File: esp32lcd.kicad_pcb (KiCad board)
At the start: 2 copper layers, 78 x 44 mm, 26 parts, among them J101 USB_B_Micro, J102 Barrel_Jack_Switch, Q102 MMBT5551, Q103 MMBT5551, Q107 MMBT5401, U101 SRV05-4, U102 CH340C, U105 AMS1117-3.3, U106 ESP32-WROOM-32D, U107 ILI9341_SPI_Touch_SD

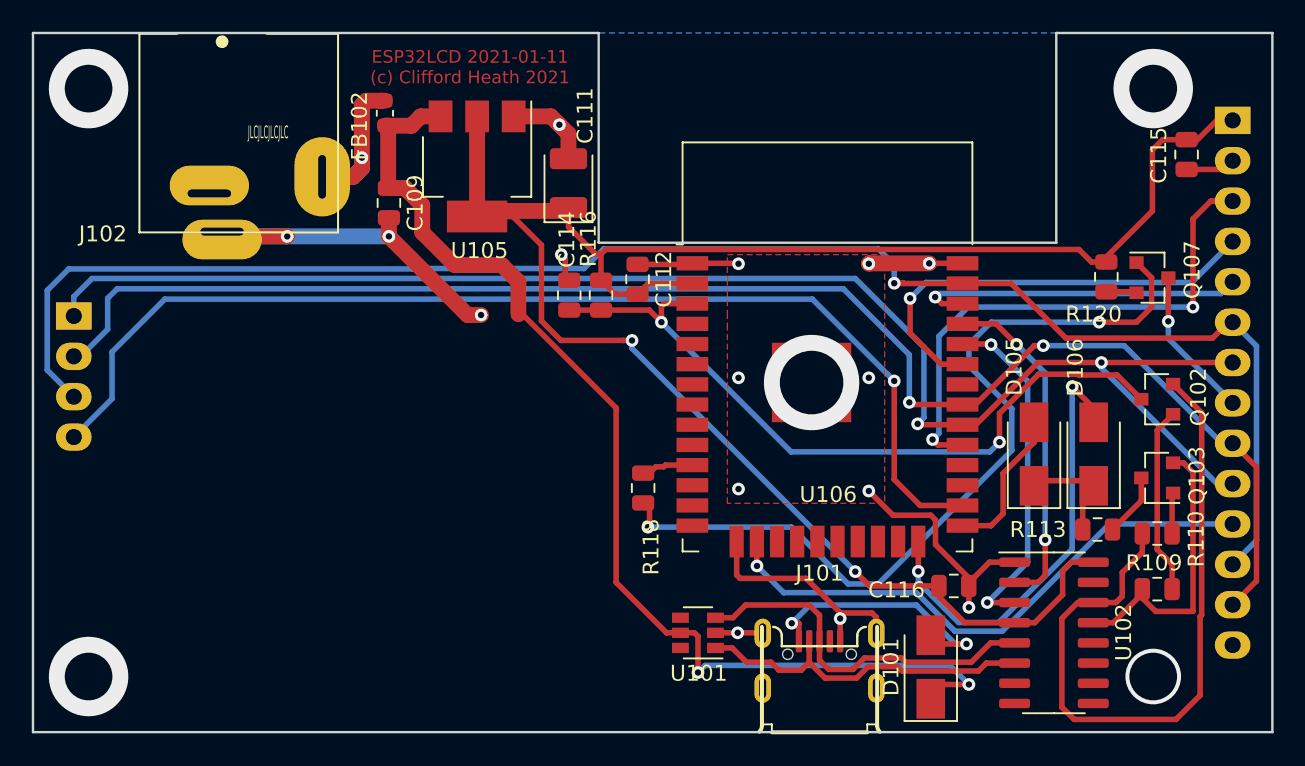
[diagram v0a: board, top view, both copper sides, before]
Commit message: Switched TxD and RxD between the two chips
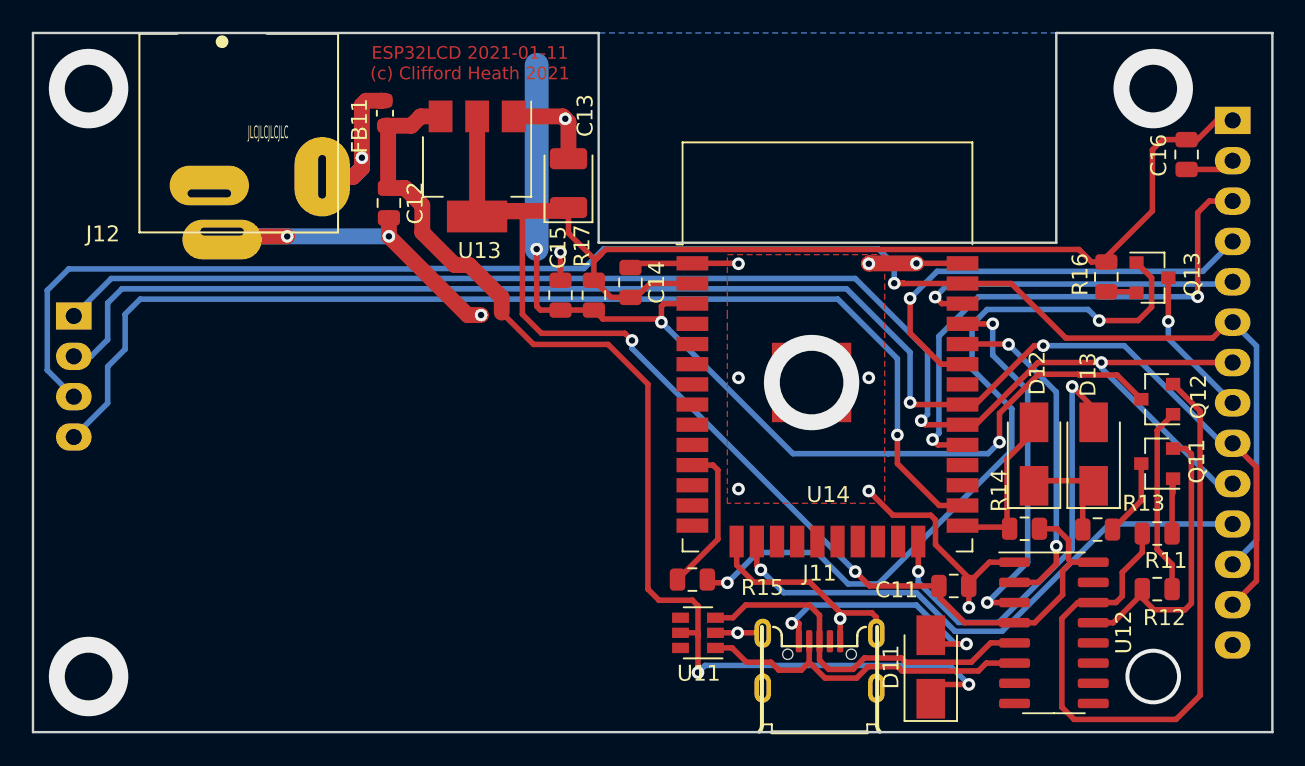
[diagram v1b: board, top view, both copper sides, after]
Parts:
- removed D105: SS14, Diode_SMD:D_SMA
- removed R109, R113: 10k, Resistor_SMD:R_0805_2012Metric
- added D12: SS14, Diode_SMD:D_SMA, F.Cu at (138.0, 137.5)
- added R12: 10k, Resistor_SMD:R_0805_2012Metric, F.Cu at (145.8, 146.0)
- added R13: 10k, Resistor_SMD:R_0805_2012Metric, F.Cu at (142.0, 142.2)
- added R14: 10k, Resistor_SMD:R_0805_2012Metric, F.Cu at (137.4, 142.2)
- moved R15 6.54 mm to (116.5, 145.4), turned to 0 degrees
- moved Q11 0.90 mm to (145.8, 138.1)
- moved C15 0.55 mm to (108.2, 127.5)
- moved C14 0.49 mm to (112.6, 126.7)
- moved R17 0.45 mm to (110.3, 127.5)
- renumbered C116 to C11, C109 to C12, C111 to C13, C112 to C14, C114 to C15, C115 to C16, D101 to D11, D106 to D13, FB102 to FB11, J101 to J11, J102 to J12, Q103 to Q11, Q102 to Q12, Q107 to Q13, R110 to R11, R118 to R15, R120 to R16, R116 to R17, U101 to U11, U102 to U12, U105 to U13, U106 to U14, U107 to U15
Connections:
- U12 pad 2: /TXD0 -> /RXD0
- U12 pad 3: /RXD0 -> /TXD0
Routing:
- net ESP_EN: track 46.7 -> 63.6 mm, vias 2 -> 3
- net Net-(R15-Pad1): track 2.91 -> 9.68 mm
- net +3V3: track 126.1 -> 132.0 mm
- net Net-(Q13-Pad1): track 52.9 -> 48.8 mm
- net +5V: track 69.8 -> 72.5 mm
- net /TXD0: track 21.3 -> 23.1 mm
- net Net-(Q11-Pad1): track 2.58 -> 4.38 mm
- net VSPICS1: track 70.3 -> 71.4 mm
- net Net-(D12-Pad2): track 9.43 -> 10.5 mm
- net VSPICLK: track 95.1 -> 94.1 mm
- net Net-(Q11-Pad3): track 4.00 -> 4.90 mm
- net /RXD0: track 21.8 -> 21.1 mm
- net GND: track 86.4 -> 87.0 mm

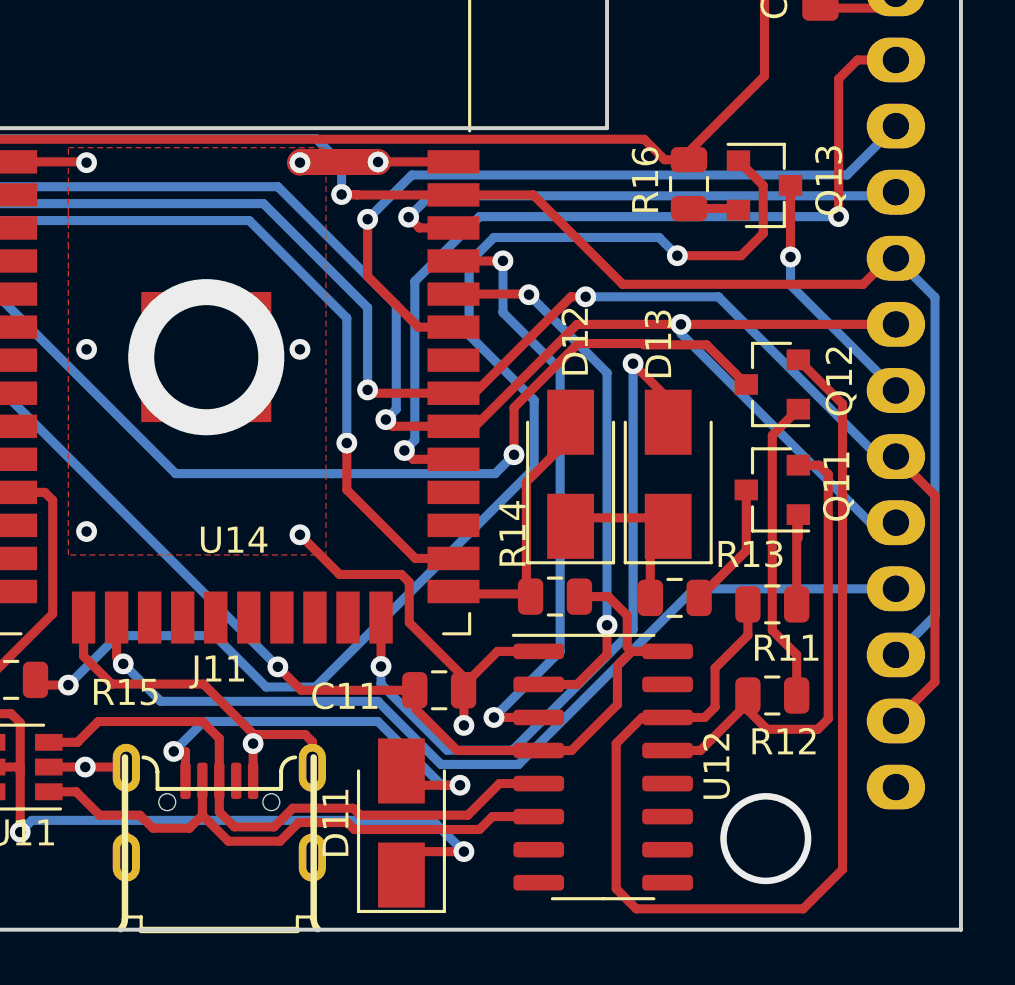
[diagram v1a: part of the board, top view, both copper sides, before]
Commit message: Ditched diode steering in favour of another transistor
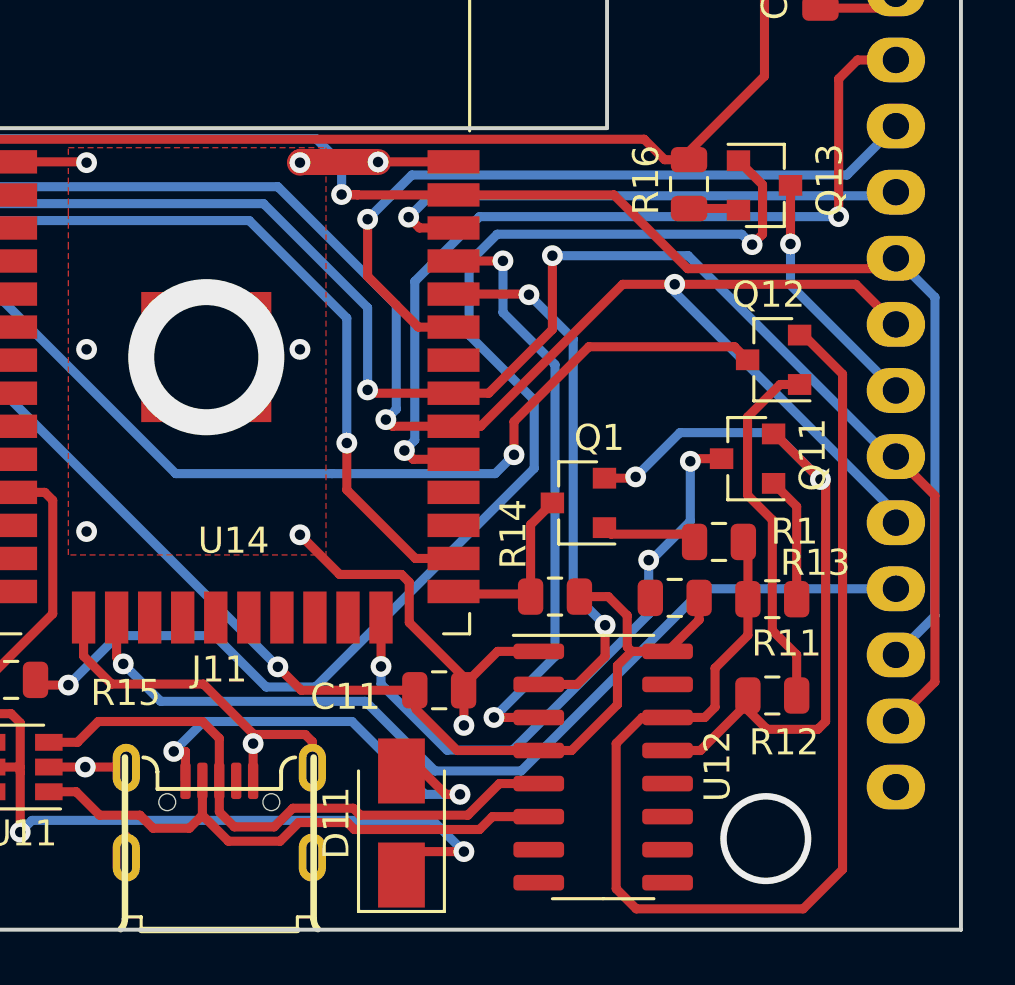
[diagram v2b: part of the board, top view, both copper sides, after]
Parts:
- removed D12, D13: SS14, Diode_SMD:D_SMA
- added Q1: MMBT5551, cjh_jlcpcb:SOT-23, F.Cu at (138.3, 138.6)
- added R1: 10k, Resistor_SMD:R_0805_2012Metric, F.Cu at (143.7, 140.1)
- R13, R14: value 10k -> 100k
- moved Q11 1.53 mm to (144.8, 136.9)
- moved Q12 0.95 mm to (145.8, 133.1)
- moved R11 0.20 mm to (145.8, 142.3)
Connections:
- R13 pad 1: Net-(Q11-Pad3) -> +3V3
- R13 pad 2: Net-(D12-Pad1) -> Net-(Q11-Pad3)
- U14 pad 24: Net-(D13-Pad2) -> Net-(Q11-Pad3)
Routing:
- net Net-(D13-Pad2): track 28.2 -> 0.00 mm, vias 2 -> 0
- net Net-(Q11-Pad3): track 4.90 -> 23.9 mm, vias 0 -> 3
- net Net-(Q1-Pad2): track 18.9 -> 30.1 mm, vias 0 -> 2
- net Net-(D12-Pad1): track 7.05 -> 0.00 mm
- net Net-(Q1-Pad1): track 0.00 -> 3.69 mm
- net Net-(Q12-Pad2): track 44.4 -> 47.9 mm
- net Net-(Q1-Pad3): track 10.5 -> 7.22 mm
- net VSPIDIN: track 96.4 -> 99.4 mm
- net +3V3: track 132.0 -> 134.6 mm
- net VSPICLK: track 94.1 -> 96.4 mm
- net Net-(Q12-Pad1): track 11.8 -> 14.0 mm
- net ESP_EN: track 63.6 -> 62.8 mm
- net Net-(Q11-Pad1): track 4.38 -> 5.02 mm

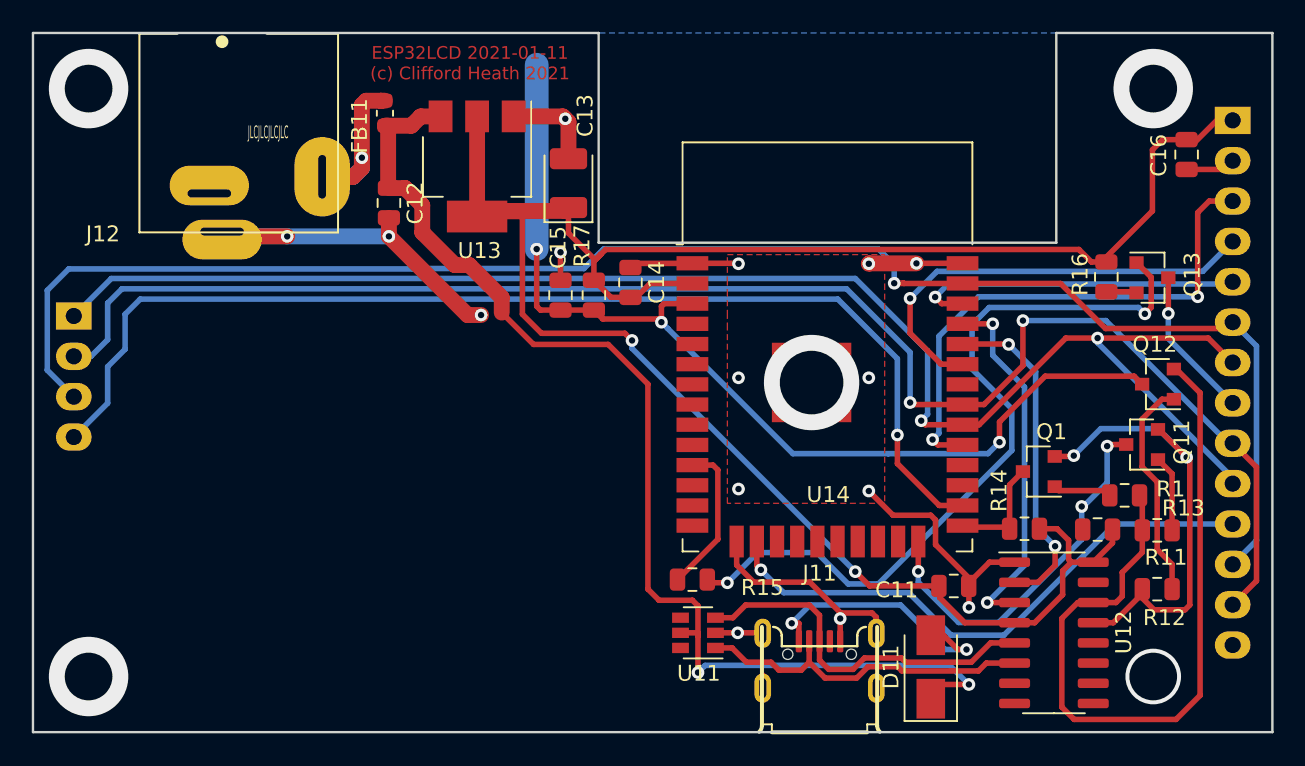
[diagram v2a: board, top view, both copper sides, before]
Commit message: Deleted GPIO2 boot pulldown
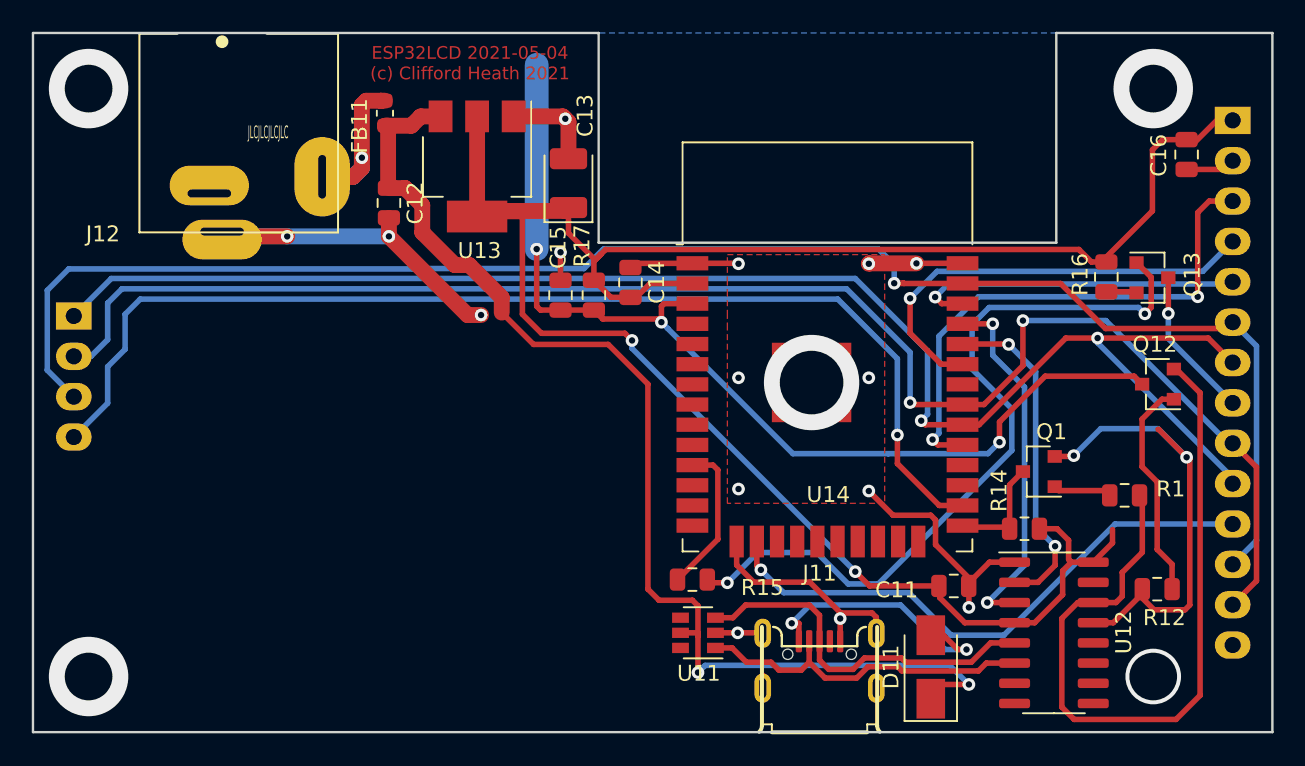
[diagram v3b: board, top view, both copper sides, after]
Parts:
- removed Q11: MMBT5551, cjh_jlcpcb:SOT-23
- removed R11: 10k, Resistor_SMD:R_0805_2012Metric
- removed R13: 100k, Resistor_SMD:R_0805_2012Metric
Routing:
- net Net-(U14-Pad24): track 23.9 -> 0.00 mm, vias 3 -> 0
- net Net-(Q11-Pad1): track 5.02 -> 0.00 mm
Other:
- board text added: "ESP32LCD 2021-05-04 (c) Clifford Heath 2021"
- board text removed: "ESP32LCD 2021-01-11 (c) Clifford Heath 2021"

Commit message: Updated to add JTAG debug
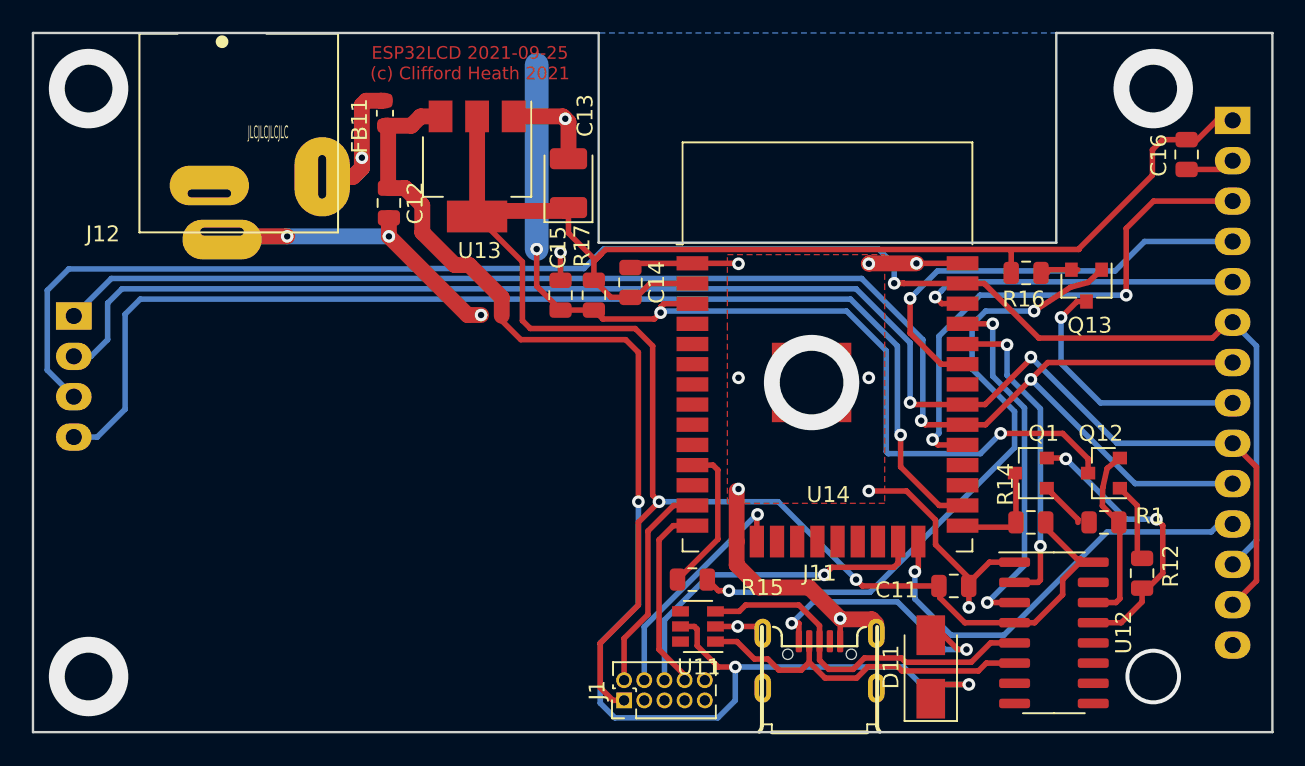
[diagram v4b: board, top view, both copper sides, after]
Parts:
- added J1: Conn_02x05_Odd_Even, Connector_PinHeader_1.27mm:PinHeader_2x05_P1.27mm_Vertical, F.Cu at (112.2, 153.0)
- moved Q12 6.55 mm to (142.4, 138.7)
- moved R16 5.06 mm to (137.5, 126.1), turned to 180 degrees
- moved Q13 4.18 mm to (141.3, 126.9), turned to 90 degrees
- moved R1 2.14 mm to (142.4, 141.8)
- moved R12 1.38 mm to (144.8, 145.0), turned to 90 degrees
- moved R14 0.57 mm to (137.8, 141.8)
- moved Q1 0.51 mm to (137.8, 138.7)
- moved U11 0.40 mm to (116.8, 148.3)
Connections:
- U14 pad 16: VSPICS2 -> Net-(J1-Pad4)
- U14 pad 24: Net-(U14-Pad24) -> VSPICS2
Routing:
- net Net-(Q12-Pad2): track 47.9 -> 11.5 mm
- net Net-(J1-Pad6): track 0.00 -> 21.3 mm, vias 0 -> 1
- net +3V3: track 134.6 -> 150.3 mm
- net Net-(J1-Pad4): track 0.00 -> 15.1 mm, vias 0 -> 1
- net +5V: track 72.5 -> 86.6 mm, vias 2 -> 3
- net Net-(J1-Pad2): track 0.00 -> 13.5 mm
- net Net-(J1-Pad8): track 0.00 -> 12.0 mm
- net Net-(Q1-Pad2): track 30.1 -> 18.2 mm
- net Net-(Q12-Pad1): track 14.0 -> 4.99 mm
- net VSPICS2: track 36.2 -> 27.5 mm
- net BACKLIGHT: track 10.5 -> 17.7 mm
- net Net-(Q13-Pad1): track 48.5 -> 41.6 mm
- net VSPIDIN: track 99.4 -> 96.2 mm
- net GND: track 87.0 -> 90.0 mm
- net ESP_EN: track 62.8 -> 61.3 mm
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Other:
- board text added: "ESP32LCD 2021-09-25 (c) Clifford Heath 2021"
- board text removed: "ESP32LCD 2021-05-04 (c) Clifford Heath 2021"
